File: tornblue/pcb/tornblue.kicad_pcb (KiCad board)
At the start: 2 copper layers, 140.7 x 102.9 mm, 78 parts, among them J1 BATT, J2 SWD, J3 BREAKOUT, J4 USB C - USB2.0, Q1 AO3401A, Q2 AO3401A, SW1 SW_Push, SW10 SW_Push, SW11 SW_Push, SW12 SW_Push, SW13 SW_Push, SW14 SW_Push, SW15 SW_Push, SW16 SW_Push, SW17 SW_Push, SW18 SW_Push, SW19 EC11, SW2 SW_Push, SW20 SW_Push, SW21 SW_Push, SW22 EC11, SW23 RESET, SW3 SW_Push, SW4 SW_Push, SW5 SW_Push, SW6 SW_Push, SW7 SW_Push, SW8 SW_Push, SW9 SW_Push, U1 XC6220, U2 TP4056, U3 nRF52840_holyiot_18010, U4 SRV05-4

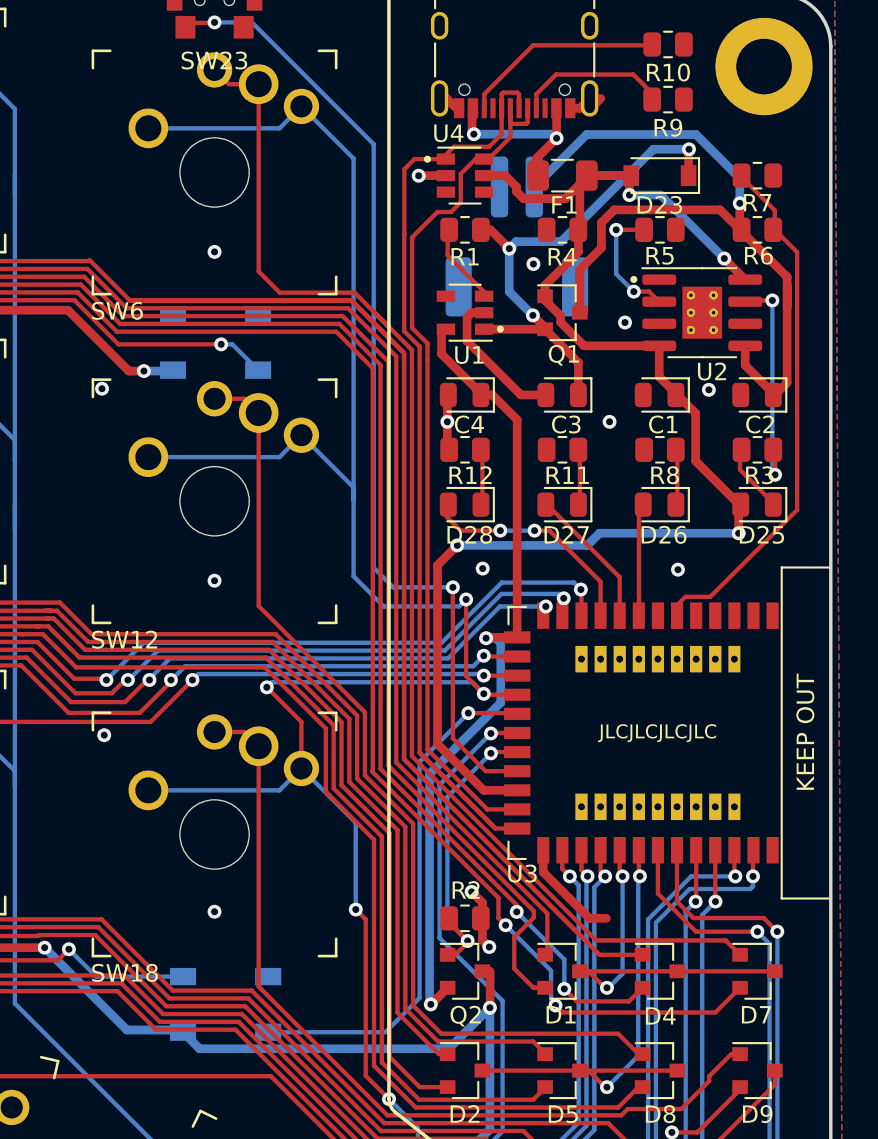
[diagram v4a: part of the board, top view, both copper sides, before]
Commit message: Move holyiot module up 1.5mm
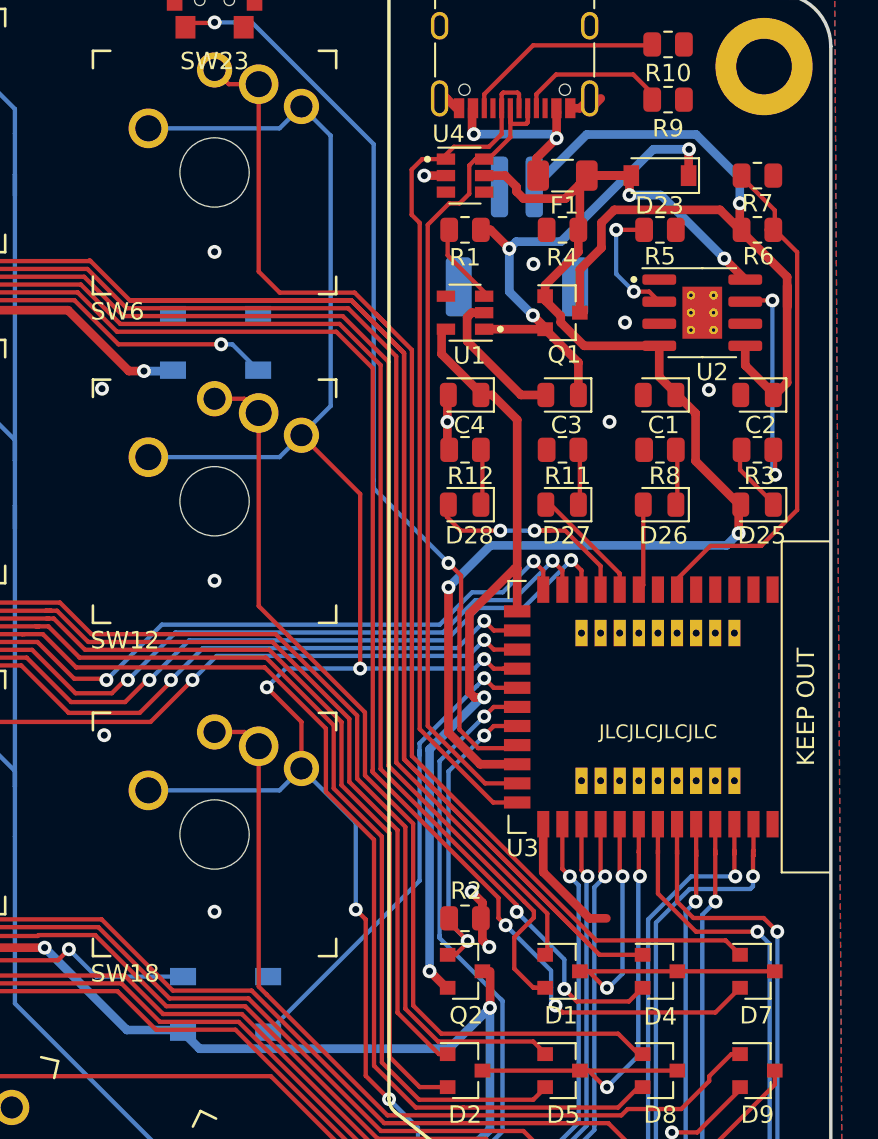
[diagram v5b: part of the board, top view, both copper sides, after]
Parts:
- moved U3 1.50 mm to (212.7, 93.1)
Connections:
- U3 pad 11: COL0 -> COL2
- U3 pad 13: COL2 -> COL0
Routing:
- net COL5: track 161.7 -> 151.7 mm
- net USB-D+: track 57.9 -> 50.0 mm
- net COL2: track 204.8 -> 208.8 mm
- net +5V: track 84.5 -> 81.5 mm
- net Net-(SW23-Pad1): track 56.7 -> 53.8 mm
- net +3V3: track 46.5 -> 49.1 mm
- net LED_DATA: track 29.9 -> 27.8 mm
- net COL0: track 195.1 -> 193.0 mm
- net ENC_B: track 110.7 -> 112.5 mm
- net ROW2: track 33.1 -> 34.9 mm
- net USB-D-: track 49.8 -> 48.0 mm
- net ROW3: track 32.0 -> 33.7 mm
- net Net-(J2-Pad3): track 28.2 -> 29.9 mm
- net ENC_A: track 104.4 -> 106.1 mm
- net Net-(J2-Pad2): track 30.1 -> 31.7 mm
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
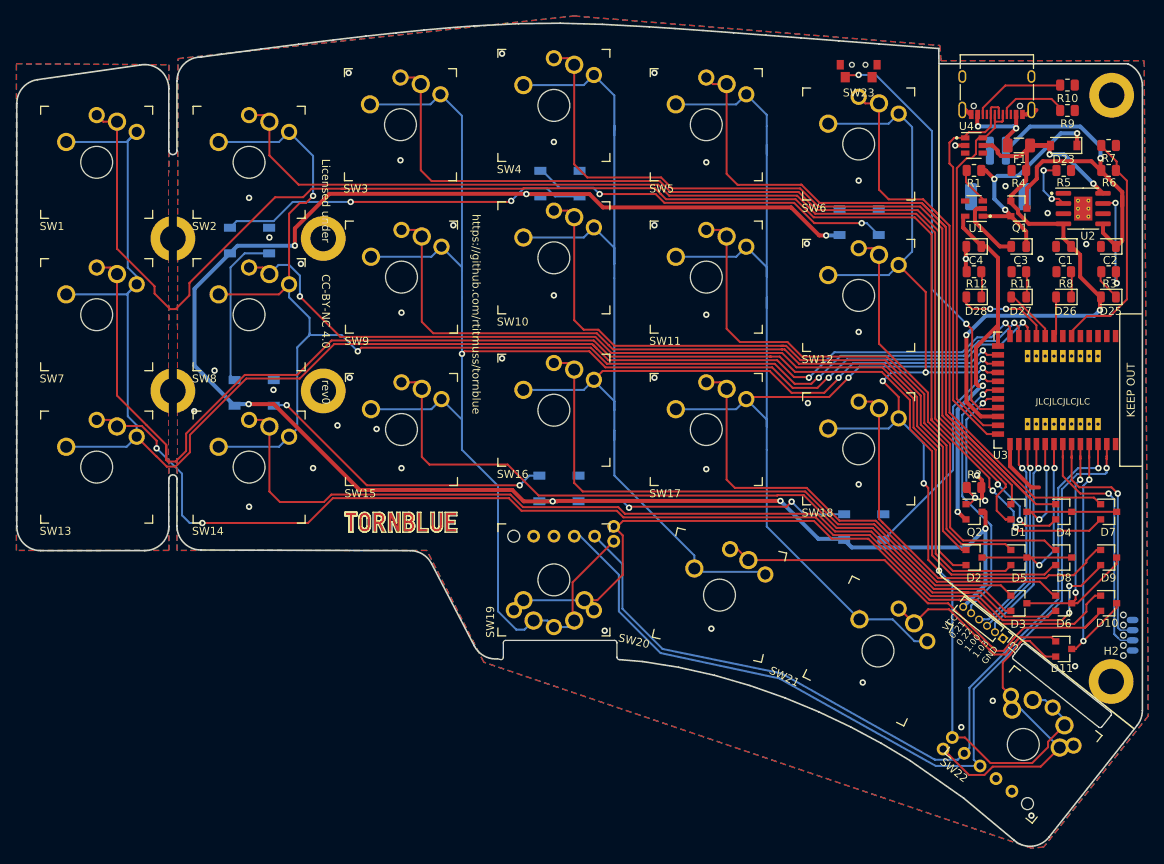
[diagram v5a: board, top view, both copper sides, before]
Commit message: Rearrange BAV70 grid
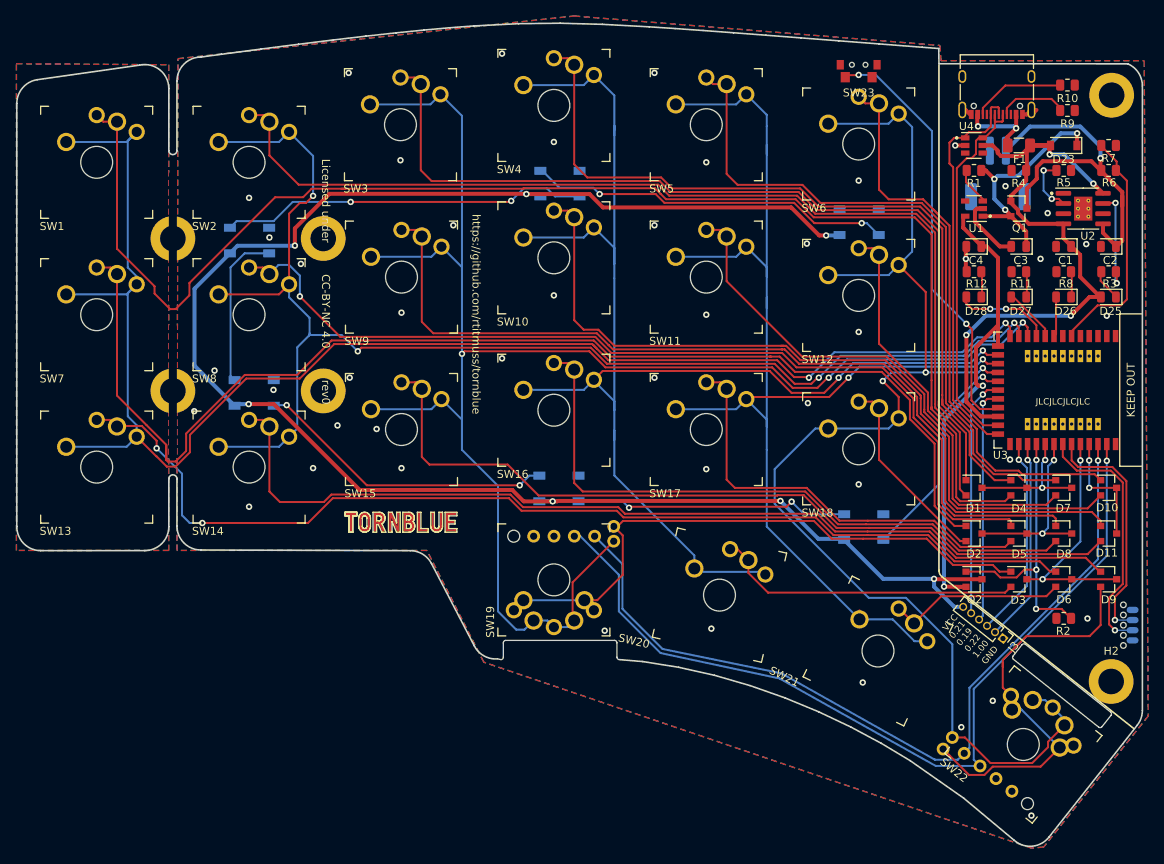
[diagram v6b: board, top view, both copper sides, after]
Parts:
- moved R2 19.8 mm to (211.9, 121.7), turned to 0 degrees
- moved D11 15.5 mm to (217.6, 111.0)
- moved D10 14.4 mm to (217.6, 105.3)
- moved Q2 8.43 mm to (200.7, 116.8)
- moved D7 6.36 mm to (211.9, 105.3)
- moved D4 6.36 mm to (206.3, 105.3)
- moved D1 6.36 mm to (200.7, 105.3)
- moved D2 3.00 mm to (200.7, 111.0)
- moved D3 3.00 mm to (206.3, 116.8)
- moved D5 3.00 mm to (206.3, 111.0)
- moved D6 3.00 mm to (211.9, 116.8)
- moved D8 3.00 mm to (211.9, 111.0)
- moved D9 2.71 mm to (217.6, 116.8)
- moved J2 1.26 mm to (221.3, 122.5)
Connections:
- SW1 pad 2: Net-(D7-Pad2) -> Net-(D4-Pad2)
- SW10 pad 2: Net-(D2-Pad1) -> Net-(D11-Pad1)
- SW11 pad 2: Net-(D5-Pad1) -> Net-(D10-Pad2)
- SW12 pad 2: Net-(D8-Pad1) -> Net-(D7-Pad2)
- SW13 pad 2: Net-(D9-Pad2) -> Net-(D6-Pad1)
- SW14 pad 2: Net-(D6-Pad2) -> Net-(D9-Pad1)
- SW15 pad 2: Net-(D3-Pad2) -> Net-(D11-Pad2)
- SW16 pad 2: Net-(D3-Pad1) -> Net-(D8-Pad2)
- SW17 pad 2: Net-(D6-Pad1) -> Net-(D5-Pad2)
- SW18 pad 2: Net-(D9-Pad1) -> Net-(D2-Pad2)
- SW19 pad S1: Net-(D10-Pad1) -> Net-(D3-Pad1)
- SW2 pad 2: Net-(D4-Pad2) -> Net-(D1-Pad2)
- SW20 pad 2: Net-(D10-Pad2) -> Net-(D3-Pad2)
- SW21 pad 2: Net-(D11-Pad1) -> Net-(D6-Pad2)
- SW22 pad S1: Net-(D11-Pad2) -> Net-(D9-Pad2)
- SW3 pad 2: Net-(D1-Pad2) -> Net-(D1-Pad1)
- SW4 pad 2: Net-(D1-Pad1) -> Net-(D4-Pad1)
- SW5 pad 2: Net-(D4-Pad1) -> Net-(D7-Pad1)
- SW6 pad 2: Net-(D7-Pad1) -> Net-(D10-Pad1)
- SW7 pad 2: Net-(D8-Pad2) -> Net-(D2-Pad1)
- SW8 pad 2: Net-(D5-Pad2) -> Net-(D5-Pad1)
- SW9 pad 2: Net-(D2-Pad2) -> Net-(D8-Pad1)
- U3 pad 20: ENABLE -> GPIO_C
- U3 pad 26: GPIO_C -> GPIO_A
- U3 pad 27: GPIO_A -> GPIO_B
- U3 pad 28: GPIO_B -> ENABLE
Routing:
- net Net-(D7-Pad2): track 186.7 -> 51.4 mm, vias 2 -> 0
- net Net-(D6-Pad2): track 117.5 -> 22.3 mm
- net Net-(D9-Pad2): track 147.0 -> 53.1 mm, vias 4 -> 0
- net Net-(D8-Pad2): track 171.6 -> 81.7 mm
- net Net-(D2-Pad2): track 104.1 -> 24.6 mm
- net Net-(D11-Pad1): track 24.8 -> 98.9 mm
- net Net-(D6-Pad1): track 62.0 -> 134.0 mm, vias 0 -> 2
- net Net-(D9-Pad1): track 49.3 -> 119.9 mm
- net Net-(D5-Pad2): track 123.7 -> 54.4 mm, vias 1 -> 0
- net Net-(D2-Pad1): track 85.2 -> 153.8 mm
- net Net-(D11-Pad2): track 42.1 -> 102.1 mm
- net Net-(D8-Pad1): track 54.8 -> 110.0 mm
- net Net-(D3-Pad2): track 93.2 -> 38.6 mm
- net Net-(D5-Pad1): track 69.7 -> 117.6 mm, vias 0 -> 1
- net Net-(D4-Pad1): track 141.4 -> 102.0 mm
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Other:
- board text added: "0.19"
- board text removed: "1.03"

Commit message: Move BAV70 grid up 0.5mm
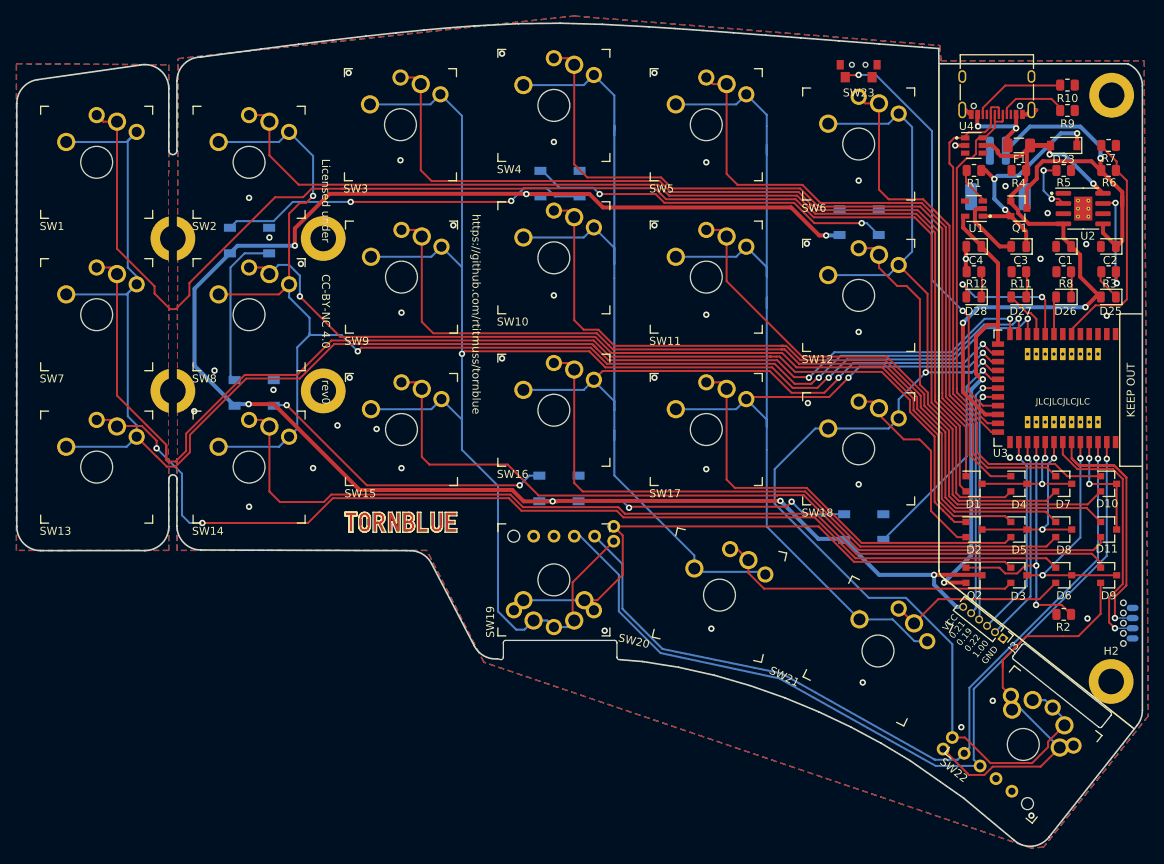
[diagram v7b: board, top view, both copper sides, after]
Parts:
- moved D1 0.50 mm to (200.7, 104.8)
- moved D10 0.50 mm to (217.6, 104.8)
- moved D11 0.50 mm to (217.6, 110.5)
- moved D2 0.50 mm to (200.7, 110.5)
- moved D3 0.50 mm to (206.3, 116.3)
- moved D4 0.50 mm to (206.3, 104.8)
- moved D5 0.50 mm to (206.3, 110.5)
- moved D6 0.50 mm to (211.9, 116.3)
- moved D7 0.50 mm to (211.9, 104.8)
- moved D8 0.50 mm to (211.9, 110.5)
- moved D9 0.50 mm to (217.6, 116.3)
- moved Q2 0.50 mm to (200.7, 116.3)
- moved R2 0.50 mm to (211.9, 121.2)
- moved J2 0.25 mm to (221.3, 122.3)
- moved U3 0.25 mm to (212.7, 92.9)
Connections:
- U3 pad 10: LED3 -> LED2
- U3 pad 9: LED2 -> LED3
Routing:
- net Net-(J2-Pad3): track 30.1 -> 43.1 mm
- net LED3: track 12.9 -> 18.0 mm
- net COL5: track 163.3 -> 159.9 mm, vias 3 -> 2
- net Net-(D1-Pad1): track 115.4 -> 114.3 mm
- net Net-(D2-Pad2): track 24.6 -> 25.7 mm
- net Net-(D8-Pad1): track 110.0 -> 108.9 mm
- net +5V: track 80.7 -> 81.6 mm
- net Net-(D11-Pad1): track 98.9 -> 98.0 mm
- net Net-(D5-Pad1): track 117.6 -> 116.7 mm
- net Net-(D4-Pad1): track 102.0 -> 101.1 mm
- net COL0: track 193.0 -> 193.8 mm
- net COL1: track 168.8 -> 169.6 mm
- net LED_DATA: track 27.9 -> 28.7 mm
- net Net-(SW23-Pad1): track 53.8 -> 53.0 mm
- net COL2: track 208.8 -> 209.5 mm
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
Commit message: Fix EVQWGD001 footprint
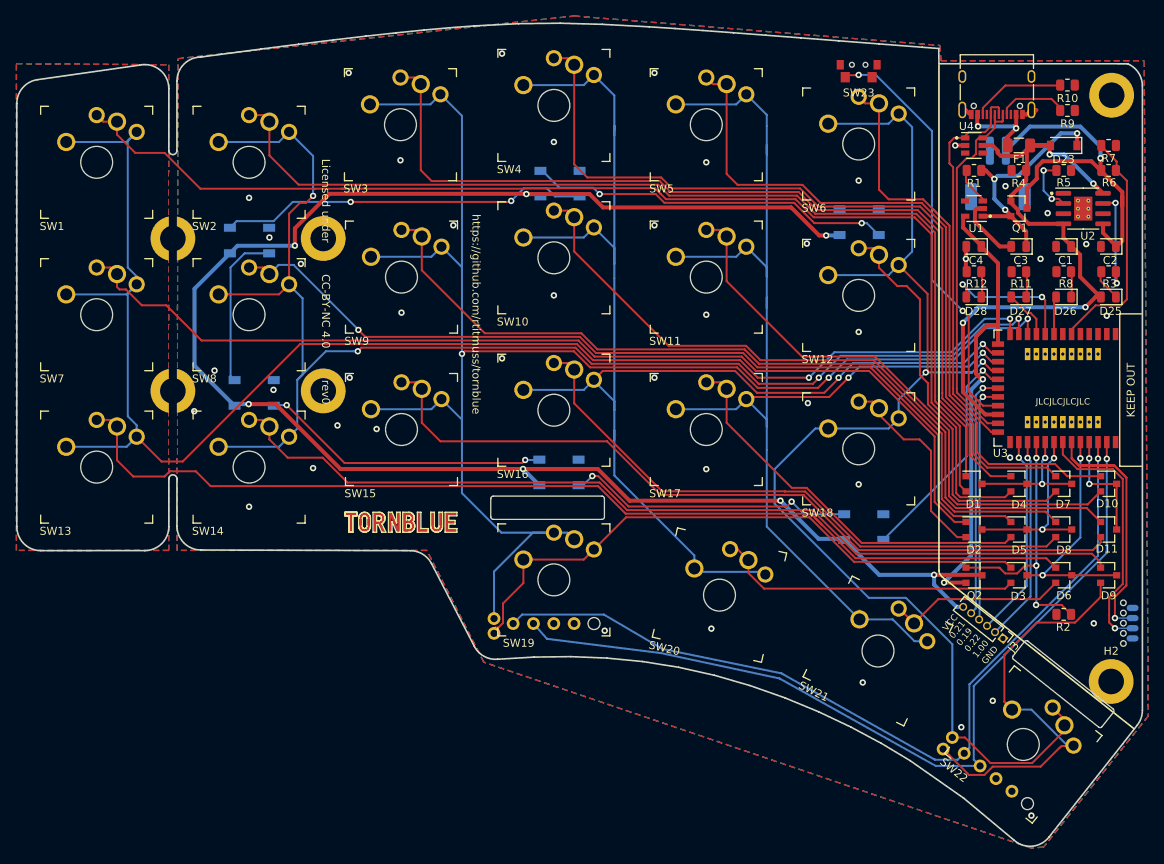
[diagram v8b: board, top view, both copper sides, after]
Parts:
- moved D13 2.00 mm to (148.8, 103.4)
- turned SW19 to 0 degrees
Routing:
- net Net-(D2-Pad1): track 153.3 -> 127.6 mm
- net Net-(D4-Pad2): track 175.2 -> 152.9 mm
- net COL2: track 209.5 -> 200.6 mm
- net Net-(D11-Pad1): track 98.0 -> 91.8 mm
- net Net-(D8-Pad2): track 81.5 -> 75.7 mm
- net Net-(D8-Pad1): track 108.9 -> 104.2 mm
- net Net-(D9-Pad1): track 120.1 -> 115.5 mm
- net Net-(D5-Pad2): track 54.2 -> 50.0 mm
- net ENC_A: track 104.6 -> 107.4 mm
- net ENC_B: track 110.4 -> 107.7 mm
- net Net-(D11-Pad2): track 102.3 -> 99.7 mm
- net Net-(D5-Pad1): track 116.7 -> 114.2 mm
- net COL0: track 193.8 -> 191.4 mm
- net COL5: track 159.9 -> 157.8 mm
- net Net-(D6-Pad1): track 133.8 -> 131.8 mm, vias 2 -> 0
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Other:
- outline, holes or cut-outs redrawn
